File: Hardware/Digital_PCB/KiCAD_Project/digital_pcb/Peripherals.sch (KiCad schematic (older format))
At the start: 14 parts, among them U2 BNO055, U3 HTU21D, Y2 32.768kHz

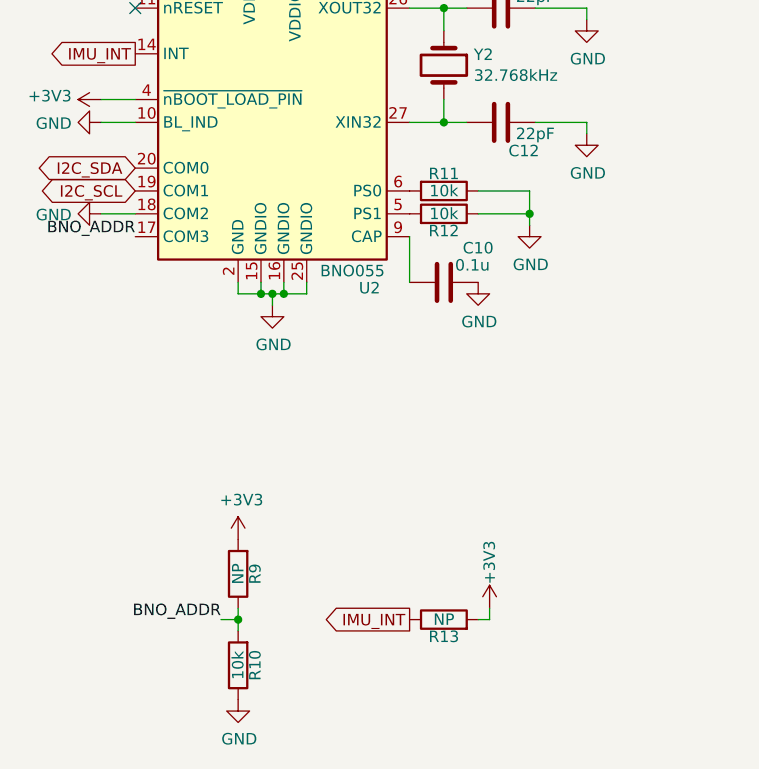
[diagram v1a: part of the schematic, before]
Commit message: Digital PCB Rev 1.0 complete.
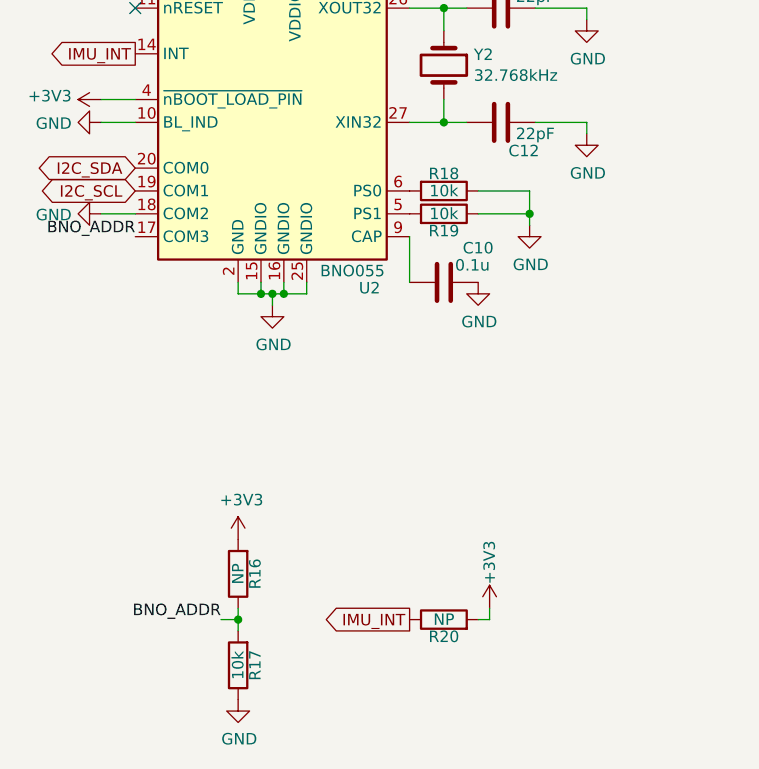
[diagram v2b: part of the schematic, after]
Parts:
- renumbered R9 to R16, R10 to R17, R11 to R18, R12 to R19, R13 to R20
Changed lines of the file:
@@
 Sheet 2 5
 Title "Digital Rotating Electronics - NSSL EFM"
-Date "2019-11-26"
+Date "2019-12-30"
 Rev "1.0"
 Comp "Leeman Geophysical LLC"
@@
 	3650 2700 3625 2700
 $Comp
-L power:GND #PWR022
+L power:GND #PWR031
 U 1 1 5DFD929D
 P 3750 4400
-F 0 "#PWR022" H 3750 4150 50  0001 C CNN
+F 0 "#PWR031" H 3750 4150 50  0001 C CNN
 F 1 "GND" H 3755 4227 50  0000 C CNN
 F 2 "" H 3750 4400 50  0001 C CNN
@@
 $EndComp
 $Comp
-L power:GND #PWR018
+L power:GND #PWR027
 U 1 1 5DFD9B68
 P 3325 2700
-F 0 "#PWR018" H 3325 2450 50  0001 C CNN
+F 0 "#PWR027" H 3325 2450 50  0001 C CNN
 F 1 "GND" H 3330 2527 50  0000 C CNN
 F 2 "" H 3325 2700 50  0001 C CNN
@@
 $EndComp
 $Comp
-L power:GND #PWR023
+L power:GND #PWR032
 U 1 1 5DFD9FE1
 P 4175 2700
-F 0 "#PWR023" H 4175 2450 50  0001 C CNN
+F 0 "#PWR032" H 4175 2450 50  0001 C CNN
 F 1 "GND" H 4180 2527 50  0000 C CNN
 F 2 "" H 4175 2700 50  0001 C CNN
@@
 $EndComp
 $Comp
-L power:+3V3 #PWR021
+L power:+3V3 #PWR030
 U 1 1 5DFDA366
 P 3750 2500
-F 0 "#PWR021" H 3750 2350 50  0001 C CNN
+F 0 "#PWR030" H 3750 2350 50  0001 C CNN
 F 1 "+3V3" H 3765 2673 50  0000 C CNN
 F 2 "" H 3750 2500 50  0001 C CNN
@@
 $EndComp
 $Comp
-L power:GND #PWR024
+L power:GND #PWR033
 U 1 1 5DFDB36A
 P 4650 4300
-F 0 "#PWR024" H 4650 4050 50  0001 C CNN
+F 0 "#PWR033" H 4650 4050 50  0001 C CNN
 F 1 "GND" H 4655 4127 50  0000 C CNN
 F 2 "" H 4650 4300 50  0001 C CNN
@@
 $EndComp
 $Comp
-L Device:R R11
+L Device:R R18
 U 1 1 5DFDB705
 P 4500 3900
-F 0 "R11" V 4425 3900 50  0000 C CNN
+F 0 "R18" V 4425 3900 50  0000 C CNN
 F 1 "10k" V 4500 3900 50  0000 C CNN
 F 2 "Resistors_SMD:R_0603_HandSoldering" V 4430 3900 50  0001 C CNN
@@
 	4350 4300 4350 4100
 $Comp
-L Device:R R12
+L Device:R R19
 U 1 1 5DFDD648
 P 4500 4000
-F 0 "R12" V 4425 4000 50  0000 C CNN
+F 0 "R19" V 4425 4000 50  0000 C CNN
 F 1 "10k" V 4500 4000 50  0000 C CNN
 F 2 "Resistors_SMD:R_0603_HandSoldering" V 4430 4000 50  0001 C CNN
@@
 $EndComp
 $Comp
-L power:GND #PWR026
+L power:GND #PWR035
 U 1 1 5DFDDB88
 P 4875 4050
-F 0 "#PWR026" H 4875 3800 50  0001 C CNN
+F 0 "#PWR035" H 4875 3800 50  0001 C CNN
 F 1 "GND" H 4880 3877 50  0000 C CNN
 F 2 "" H 4875 4050 50  0001 C CNN
@@
 	5125 3600 5125 3650
 $Comp
-L power:GND #PWR028
+L power:GND #PWR037
 U 1 1 5DFE16EA
 P 5125 3650
-F 0 "#PWR028" H 5125 3400 50  0001 C CNN
+F 0 "#PWR037" H 5125 3400 50  0001 C CNN
 F 1 "GND" H 5130 3477 50  0000 C CNN
 F 2 "" H 5125 3650 50  0001 C CNN
@@
 $EndComp
 $Comp
-L power:GND #PWR027
+L power:GND #PWR036
 U 1 1 5DFE1907
 P 5125 3150
-F 0 "#PWR027" H 5125 2900 50  0001 C CNN
+F 0 "#PWR036" H 5125 2900 50  0001 C CNN
 F 1 "GND" H 5130 2977 50  0000 C CNN
 F 2 "" H 5125 3150 50  0001 C CNN
@@
 	3700 4350 3750 4350
 $Comp
-L power:GND #PWR016
+L power:GND #PWR025
 U 1 1 5DFE4AE9
 P 3000 3600
-F 0 "#PWR016" H 3000 3350 50  0001 C CNN
+F 0 "#PWR025" H 3000 3350 50  0001 C CNN
 F 1 "GND" V 3005 3472 50  0000 R CNN
 F 2 "" H 3000 3600 50  0001 C CNN
@@
 	3000 3600 3150 3600
 $Comp
-L power:+3V3 #PWR015
+L power:+3V3 #PWR024
 U 1 1 5DFE56B9
 P 3000 3500
-F 0 "#PWR015" H 3000 3350 50  0001 C CNN
+F 0 "#PWR024" H 3000 3350 50  0001 C CNN
 F 1 "+3V3" V 3015 3628 50  0000 L CNN
 F 2 "" H 3000 3500 50  0001 C CNN
@@
 	3000 3500 3150 3500
 $Comp
-L power:GND #PWR017
+L power:GND #PWR026
 U 1 1 5DFE66D6
 P 3000 4000
-F 0 "#PWR017" H 3000 3750 50  0001 C CNN
+F 0 "#PWR026" H 3000 3750 50  0001 C CNN
 F 1 "GND" V 3005 3872 50  0000 R CNN
 F 2 "" H 3000 4000 50  0001 C CNN
@@
 BNO_ADDR
 $Comp
-L Device:R R10
+L Device:R R17
 U 1 1 5DFE72AD
 P 3600 5975
-F 0 "R10" V 3525 5975 50  0000 C CNN
+F 0 "R17" V 3525 5975 50  0000 C CNN
 F 1 "10k" V 3600 5975 50  0000 C CNN
 F 2 "Resistors_SMD:R_0603_HandSoldering" V 3530 5975 50  0001 C CNN
@@
 $EndComp
 $Comp
-L Device:R R9
+L Device:R R16
 U 1 1 5DFE79BC
 P 3600 5575
-F 0 "R9" V 3525 5575 50  0000 C CNN
+F 0 "R16" V 3525 5575 50  0000 C CNN
 F 1 "NP" V 3600 5575 50  0000 C CNN
 F 2 "Resistors_SMD:R_0603_HandSoldering" V 3530 5575 50  0001 C CNN
@@
 Connection ~ 3600 5775
 $Comp
-L power:GND #PWR020
+L power:GND #PWR029
 U 1 1 5DFE8EC2
 P 3600 6125
-F 0 "#PWR020" H 3600 5875 50  0001 C CNN
+F 0 "#PWR029" H 3600 5875 50  0001 C CNN
 F 1 "GND" H 3605 5952 50  0000 C CNN
 F 2 "" H 3600 6125 50  0001 C CNN
@@
 $EndComp
 $Comp
-L power:+3V3 #PWR019
+L power:+3V3 #PWR028
 U 1 1 5DFE9212
 P 3600 5425
-F 0 "#PWR019" H 3600 5275 50  0001 C CNN
+F 0 "#PWR028" H 3600 5275 50  0001 C CNN
 F 1 "+3V3" H 3615 5598 50  0000 C CNN
 F 2 "" H 3600 5425 50  0001 C CNN
@@
 $EndComp
 $Comp
-L power:GND #PWR029
+L power:GND #PWR038
 U 1 1 5DDD9BBE
 P 7625 2675
-F 0 "#PWR029" H 7625 2425 50  0001 C CNN
+F 0 "#PWR038" H 7625 2425 50  0001 C CNN
 F 1 "GND" H 7630 2502 50  0000 C CNN
 F 2 "" H 7625 2675 50  0001 C CNN
@@
 $EndComp
 $Comp
-L power:+3V3 #PWR030
+L power:+3V3 #PWR039
 U 1 1 5DDDA1F7
 P 7975 2625
-F 0 "#PWR030" H 7975 2475 50  0001 C CNN
+F 0 "#PWR039" H 7975 2475 50  0001 C CNN
 F 1 "+3V3" H 7990 2798 50  0000 C CNN
 F 2 "" H 7975 2625 50  0001 C CNN
@@
 I2C_SCL
 $Comp
-L power:GND #PWR031
+L power:GND #PWR040
 U 1 1 5DDDD282
 P 8025 3825
-F 0 "#PWR031" H 8025 3575 50  0001 C CNN
+F 0 "#PWR040" H 8025 3575 50  0001 C CNN
 F 1 "GND" H 8030 3652 50  0000 C CNN
 F 2 "" H 8025 3825 50  0001 C CNN
@@
 	4650 5775 4700 5775
 $Comp
-L power:+3V3 #PWR025
+L power:+3V3 #PWR034
 U 1 1 5DFE9D21
 P 4700 5725
-F 0 "#PWR025" H 4700 5575 50  0001 C CNN
+F 0 "#PWR034" H 4700 5575 50  0001 C CNN
 F 1 "+3V3" V 4700 5925 50  0000 C CNN
 F 2 "" H 4700 5725 50  0001 C CNN
@@
 $EndComp
 $Comp
-L Device:R R13
+L Device:R R20
 U 1 1 5DFE9D1B
 P 4500 5775
-F 0 "R13" V 4425 5775 50  0000 C CNN
+F 0 "R20" V 4425 5775 50  0000 C CNN
 F 1 "NP" V 4500 5775 50  0000 C CNN
 F 2 "Resistors_SMD:R_0603_HandSoldering" V 4430 5775 50  0001 C CNN

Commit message: Update IMU crystal footprint to 4-SOJ. closes #5.
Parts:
- Y2: footprint Crystals:Crystal_SMD_HC49-SD -> lib_fp:4-SOJ
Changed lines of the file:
@@
 EESchema Schematic File Version 4
-LIBS:digital_pcb-cache
 EELAYER 30 0
 EELAYER END
@@
 F 0 "Y2" V 4454 3481 50  0000 L CNN
 F 1 "32.768kHz" V 4545 3481 50  0000 L CNN
-F 2 "Crystals:Crystal_SMD_HC49-SD" H 4500 3350 50  0001 C CNN
+F 2 "lib_fp:4-SOJ" H 4500 3350 50  0001 C CNN
 F 3 "~" H 4500 3350 50  0001 C CNN
 F 4 "1-0000220" H 4500 3350 50  0001 C CNN "Internal Part Number"

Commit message: Swap sensor from T/RH to T/RH/P and update schematic version.
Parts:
- removed C13: 0.1u, Capacitors_SMD:C_0603_HandSoldering, symbol Device:C
- removed R16: NP, Resistors_SMD:R_0603_HandSoldering, symbol Device:R
- removed R17: 10k, Resistors_SMD:R_0603_HandSoldering, symbol Device:R
- removed U3: HTU21D, lib_fp:SON100P300X300X90-7N, symbol lib_sch:HTU21D
- added C? (x2): 0.1u, Capacitors_SMD:C_0603_HandSoldering, symbol Device:C
- added U?: BME280, Package_LGA:Bosch_LGA-8_2.5x2.5mm_P0.65mm_ClockwisePinNumbering, symbol Sensor:BME280
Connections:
- net labels removed: BNO_ADDR
- wire segments 42 -> 47
- no-connect marks 2 -> 1
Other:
- note added: "Address: 0x28"
- note added: "Address: 0x76"
- note added: "Temperature/Humidity/Pressure\nSensor"
- note removed: "Temperature/Humidity Sensor"
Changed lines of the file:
@@
 $EndComp
 Wire Wire Line
-	3000 4000 3150 4000
-Text Label 3150 4100 2    50   ~ 0
-BNO_ADDR
-Text Label 3525 5775 2    50   ~ 0
-BNO_ADDR
-$Comp
-L Device:R R17
-U 1 1 5DFE72AD
-P 3600 5975
-F 0 "R17" V 3525 5975 50  0000 C CNN
-F 1 "10k" V 3600 5975 50  0000 C CNN
-F 2 "Resistors_SMD:R_0603_HandSoldering" V 3530 5975 50  0001 C CNN
-F 3 "~" H 3600 5975 50  0001 C CNN
-F 4 "1-0000010" H 3600 5975 50  0001 C CNN "Internal Part Number"
-F 5 "1" H 3600 5975 50  0001 C CNN "Populated"
-	1    3600 5975
-	-1   0    0    1
-$EndComp
-$Comp
-L Device:R R16
-U 1 1 5DFE79BC
-P 3600 5575
-F 0 "R16" V 3525 5575 50  0000 C CNN
-F 1 "NP" V 3600 5575 50  0000 C CNN
-F 2 "Resistors_SMD:R_0603_HandSoldering" V 3530 5575 50  0001 C CNN
-F 3 "~" H 3600 5575 50  0001 C CNN
-F 4 "1-0000010" H 3600 5575 50  0001 C CNN "Internal Part Number"
-F 5 "0" H 3600 5575 50  0001 C CNN "Populated"
-	1    3600 5575
-	-1   0    0    1
-$EndComp
-Wire Wire Line
-	3525 5775 3600 5775
-Wire Wire Line
-	3600 5775 3600 5725
-Wire Wire Line
-	3600 5825 3600 5775
-Connection ~ 3600 5775
-$Comp
-L power:GND #PWR029
-U 1 1 5DFE8EC2
-P 3600 6125
-F 0 "#PWR029" H 3600 5875 50  0001 C CNN
-F 1 "GND" H 3605 5952 50  0000 C CNN
-F 2 "" H 3600 6125 50  0001 C CNN
-F 3 "" H 3600 6125 50  0001 C CNN
-	1    3600 6125
-	1    0    0    -1
-$EndComp
-$Comp
-L power:+3V3 #PWR028
-U 1 1 5DFE9212
-P 3600 5425
-F 0 "#PWR028" H 3600 5275 50  0001 C CNN
-F 1 "+3V3" H 3615 5598 50  0000 C CNN
-F 2 "" H 3600 5425 50  0001 C CNN
-F 3 "" H 3600 5425 50  0001 C CNN
-	1    3600 5425
-	1    0    0    -1
-$EndComp
+	3000 4000 3075 4000
 Text GLabel 3150 3300 0    50   Output ~ 0
 IMU_INT
@@
 I2C_SCL
 NoConn ~ 3150 3100
-$Comp
-L lib_sch:HTU21D U3
-U 1 1 5DDD8919
-P 7975 3275
-F 0 "U3" H 8253 3321 50  0000 L CNN
-F 1 "HTU21D" H 8253 3230 50  0000 L CNN
-F 2 "lib_fp:SON100P300X300X90-7N" H 6875 3275 50  0001 C CNN
-F 3 "" H 6875 3275 50  0001 C CNN
-F 4 "1-0000471" H 7975 3275 50  0001 C CNN "Internal Part Number"
-F 5 "1" H 7975 3275 50  0001 C CNN "Populated"
-	1    7975 3275
-	1    0    0    -1
-$EndComp
-$Comp
-L Device:C C?
-U 1 1 5DDD9BB8
-P 7775 2675
-AR Path="/5DDD9BB8" Ref="C?"  Part="1"
-AR Path="/5DFD7345/5DDD9BB8" Ref="C13"  Part="1"
-F 0 "C13" V 7625 2525 50  0000 C CNN
-F 1 "0.1u" V 7700 2550 50  0000 C CNN
-F 2 "Capacitors_SMD:C_0603_HandSoldering" H 7813 2525 50  0001 C CNN
-F 3 "~" H 7775 2675 50  0001 C CNN
-F 4 "1-0000007" H 7775 2675 50  0001 C CNN "Internal Part Number"
-F 5 "1" H 7775 2675 50  0001 C CNN "Populated"
-	1    7775 2675
-	0    1    1    0
-$EndComp
-$Comp
-L power:GND #PWR038
-U 1 1 5DDD9BBE
-P 7625 2675
-F 0 "#PWR038" H 7625 2425 50  0001 C CNN
-F 1 "GND" H 7630 2502 50  0000 C CNN
-F 2 "" H 7625 2675 50  0001 C CNN
-F 3 "" H 7625 2675 50  0001 C CNN
-	1    7625 2675
-	1    0    0    -1
-$EndComp
-$Comp
-L power:+3V3 #PWR039
-U 1 1 5DDDA1F7
-P 7975 2625
-F 0 "#PWR039" H 7975 2475 50  0001 C CNN
-F 1 "+3V3" H 7990 2798 50  0000 C CNN
-F 2 "" H 7975 2625 50  0001 C CNN
-F 3 "" H 7975 2625 50  0001 C CNN
-	1    7975 2625
-	1    0    0    -1
-$EndComp
-Wire Wire Line
-	7975 2625 7975 2675
-Wire Wire Line
-	7925 2675 7975 2675
-Connection ~ 7975 2675
-Wire Wire Line
-	7975 2675 7975 2725
-Text GLabel 7525 3225 0    50   BiDi ~ 0
-I2C_SDA
-Text GLabel 7525 3325 0    50   BiDi ~ 0
-I2C_SCL
-$Comp
-L power:GND #PWR040
-U 1 1 5DDDD282
-P 8025 3825
-F 0 "#PWR040" H 8025 3575 50  0001 C CNN
-F 1 "GND" H 8030 3652 50  0000 C CNN
-F 2 "" H 8025 3825 50  0001 C CNN
-F 3 "" H 8025 3825 50  0001 C CNN
-	1    8025 3825
-	1    0    0    -1
-$EndComp
-NoConn ~ 7925 3825
-Text Notes 6775 2075 0    100  ~ 0
-Temperature/Humidity Sensor
+Text Notes 6800 2200 0    100  ~ 0
+Temperature/Humidity/Pressure\nSensor
 Text Notes 3625 2075 0    100  ~ 0
 IMU
@@
 Text GLabel 4350 5775 0    50   Output ~ 0
 IMU_INT
+$Comp
+L Sensor:BME280 U?
+U 1 1 5FDBCAD6
+P 7825 3575
+F 0 "U?" H 8175 4050 50  0000 R CNN
+F 1 "BME280" H 7950 3575 50  0000 R CNN
+F 2 "Package_LGA:Bosch_LGA-8_2.5x2.5mm_P0.65mm_ClockwisePinNumbering" H 9325 3125 50  0001 C CNN
+F 3 "https://ae-bst.resource.bosch.com/media/_tech/media/datasheets/BST-BME280-DS002.pdf" H 7825 3375 50  0001 C CNN
+F 4 "1-0000052" H 7825 3575 50  0001 C CNN "Internal Part Number"
+F 5 "1" H 7825 3575 50  0001 C CNN "Populated"
+	1    7825 3575
+	1    0    0    -1
+$EndComp
+$Comp
+L Device:C C?
+U 1 1 5FDBD897
+P 7525 2725
+AR Path="/5FDBD897" Ref="C?"  Part="1"
+AR Path="/5DFD7345/5FDBD897" Ref="C?"  Part="1"
+F 0 "C?" V 7375 2575 50  0000 C CNN
+F 1 "0.1u" V 7450 2600 50  0000 C CNN
+F 2 "Capacitors_SMD:C_0603_HandSoldering" H 7563 2575 50  0001 C CNN
+F 3 "~" H 7525 2725 50  0001 C CNN
+F 4 "1-0000007" H 7525 2725 50  0001 C CNN "Internal Part Number"
+F 5 "1" H 7525 2725 50  0001 C CNN "Populated"
+	1    7525 2725
+	0    1    1    0
+$EndComp
+$Comp
+L power:GND #PWR?
+U 1 1 5FDBD89D
+P 7375 2725
+F 0 "#PWR?" H 7375 2475 50  0001 C CNN
+F 1 "GND" H 7380 2552 50  0000 C CNN
+F 2 "" H 7375 2725 50  0001 C CNN
+F 3 "" H 7375 2725 50  0001 C CNN
+	1    7375 2725
+	1    0    0    -1
+$EndComp
+$Comp
+L power:+3V3 #PWR?
+U 1 1 5FDBD8A3
+P 7825 2650
+F 0 "#PWR?" H 7825 2500 50  0001 C CNN
+F 1 "+3V3" H 7840 2823 50  0000 C CNN
+F 2 "" H 7825 2650 50  0001 C CNN
+F 3 "" H 7825 2650 50  0001 C CNN
+	1    7825 2650
+	1    0    0    -1
+$EndComp
+Wire Wire Line
+	7675 2725 7725 2725
+Connection ~ 7725 2725
+$Comp
+L Device:C C?
+U 1 1 5FDC0A1A
+P 8125 2725
+AR Path="/5FDC0A1A" Ref="C?"  Part="1"
+AR Path="/5DFD7345/5FDC0A1A" Ref="C?"  Part="1"
+F 0 "C?" V 7975 2575 50  0000 C CNN
+F 1 "0.1u" V 8050 2600 50  0000 C CNN
+F 2 "Capacitors_SMD:C_0603_HandSoldering" H 8163 2575 50  0001 C CNN
+F 3 "~" H 8125 2725 50  0001 C CNN
+F 4 "1-0000007" H 8125 2725 50  0001 C CNN "Internal Part Number"
+F 5 "1" H 8125 2725 50  0001 C CNN "Populated"
+	1    8125 2725
+	0    -1   1    0
+$EndComp
+$Comp
+L power:GND #PWR?
+U 1 1 5FDC0A20
+P 8275 2725
+F 0 "#PWR?" H 8275 2475 50  0001 C CNN
+F 1 "GND" H 8280 2552 50  0000 C CNN
+F 2 "" H 8275 2725 50  0001 C CNN
+F 3 "" H 8275 2725 50  0001 C CNN
+	1    8275 2725
+	-1   0    0    -1
+$EndComp
+Wire Wire Line
+	7975 2725 7925 2725
+Connection ~ 7925 2725
+Wire Wire Line
+	7725 2650 7825 2650
+Wire Wire Line
+	7725 2650 7725 2725
+Wire Wire Line
+	7825 2650 7925 2650
+Wire Wire Line
+	7925 2650 7925 2725
+Connection ~ 7825 2650
+Wire Wire Line
+	7925 2725 7925 2975
+Wire Wire Line
+	7725 2725 7725 2975
+$Comp
+L power:+3V3 #PWR?
+U 1 1 5FDC656D
+P 8425 3875
+F 0 "#PWR?" H 8425 3725 50  0001 C CNN
+F 1 "+3V3" H 8440 4048 50  0000 C CNN
+F 2 "" H 8425 3875 50  0001 C CNN
+F 3 "" H 8425 3875 50  0001 C CNN
+	1    8425 3875
+	0    1    1    0
+$EndComp
+$Comp
+L power:GND #PWR?
+U 1 1 5FDC75ED
+P 8425 3275
+F 0 "#PWR?" H 8425 3025 50  0001 C CNN
+F 1 "GND" H 8430 3102 50  0000 C CNN
+F 2 "" H 8425 3275 50  0001 C CNN
+F 3 "" H 8425 3275 50  0001 C CNN
+	1    8425 3275
+	0    -1   1    0
+$EndComp
+Text GLabel 8425 3475 2    50   BiDi ~ 0
+I2C_SCL
+Text GLabel 8425 3675 2    50   BiDi ~ 0
+I2C_SDA
+$Comp
+L power:GND #PWR?
+U 1 1 5FDC7CCA
+P 7725 4175
+F 0 "#PWR?" H 7725 3925 50  0001 C CNN
+F 1 "GND" H 7730 4002 50  0000 C CNN
+F 2 "" H 7725 4175 50  0001 C CNN
+F 3 "" H 7725 4175 50  0001 C CNN
+	1    7725 4175
+	-1   0    0    -1
+$EndComp
+$Comp
+L power:GND #PWR?
+U 1 1 5FDC8367
+P 7925 4175
+F 0 "#PWR?" H 7925 3925 50  0001 C CNN
+F 1 "GND" H 7930 4002 50  0000 C CNN
+F 2 "" H 7925 4175 50  0001 C CNN
+F 3 "" H 7925 4175 50  0001 C CNN
+	1    7925 4175
+	-1   0    0    -1
+$EndComp
+Text Notes 8125 4150 0    50   ~ 0
+Address: 0x76
+Wire Wire Line
+	3150 4100 3075 4100
+Wire Wire Line
+	3075 4100 3075 4000
+Connection ~ 3075 4000
+Wire Wire Line
+	3075 4000 3150 4000
+Text Notes 2900 4325 0    50   ~ 0
+Address: 0x28
 $EndSCHEMATC
